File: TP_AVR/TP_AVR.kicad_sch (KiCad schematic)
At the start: 30 parts, among them J1 Conn_02x20_Counter_Clockwise, M1 ProMicro, U1 74HC238, U2 74HC238

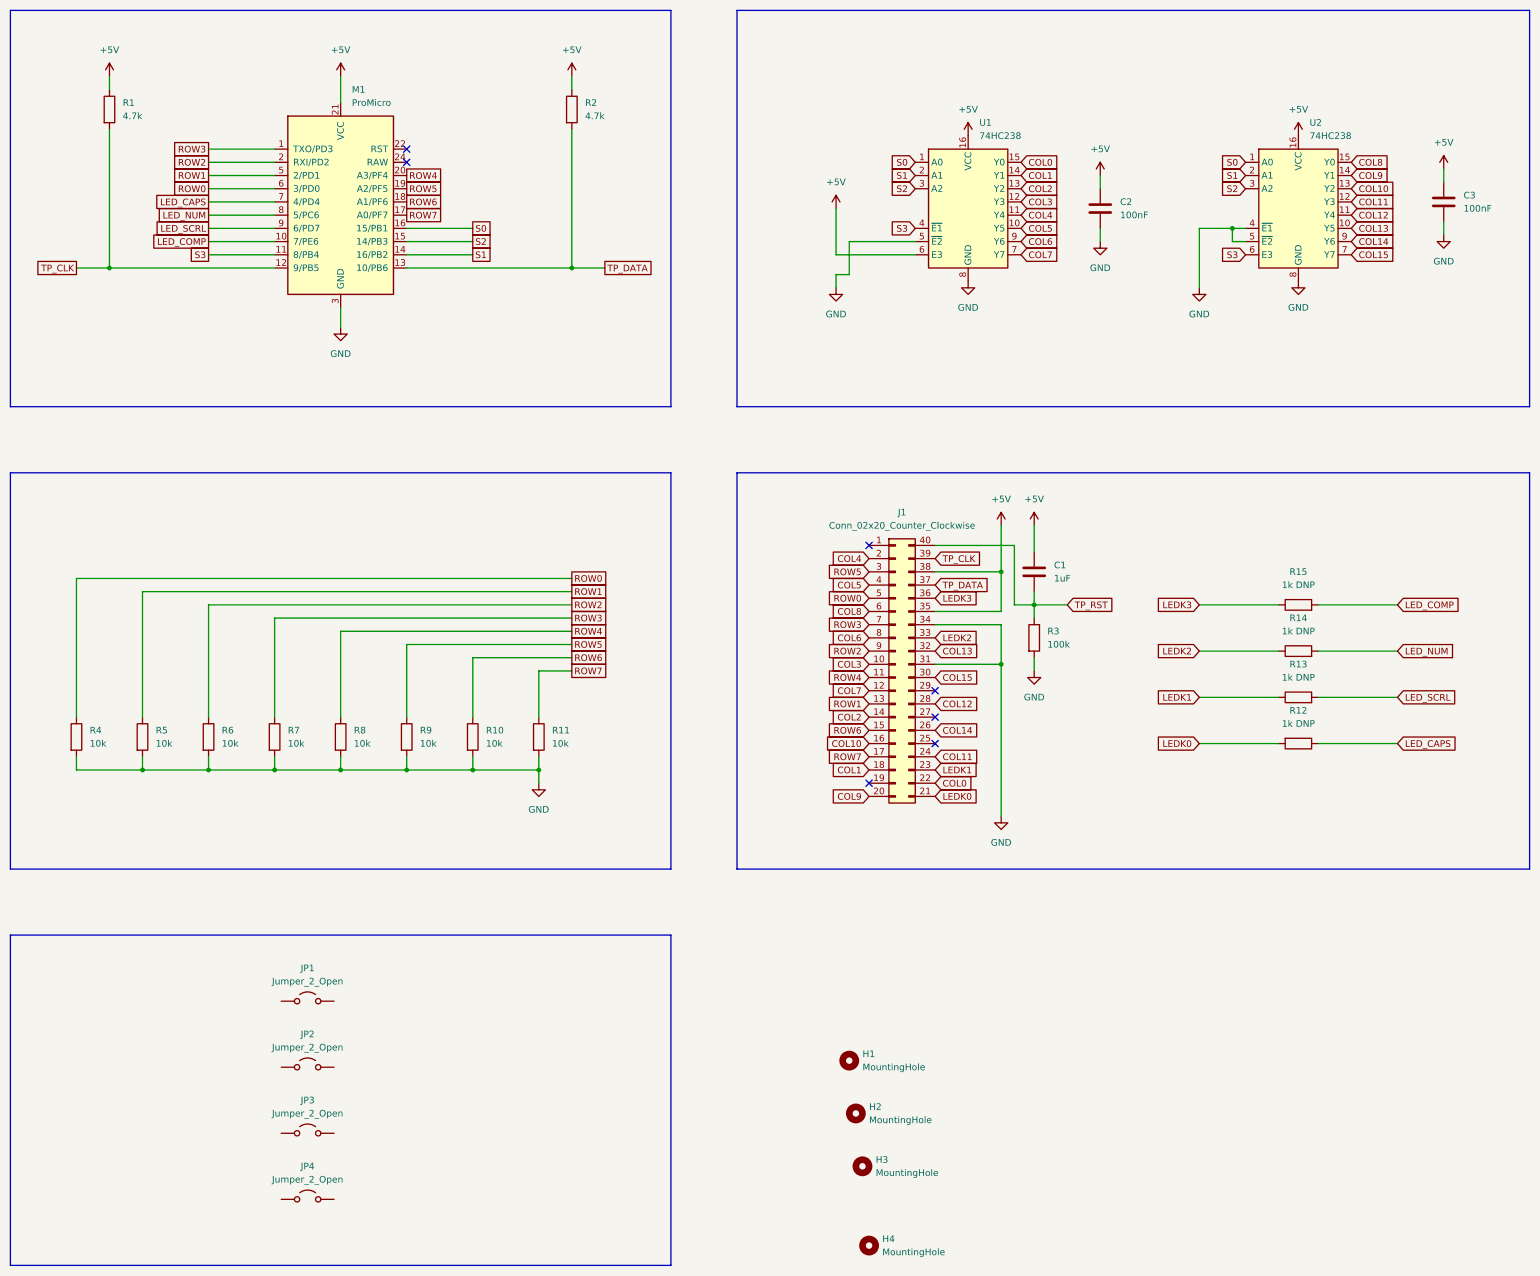
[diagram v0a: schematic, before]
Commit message: Finished up board files
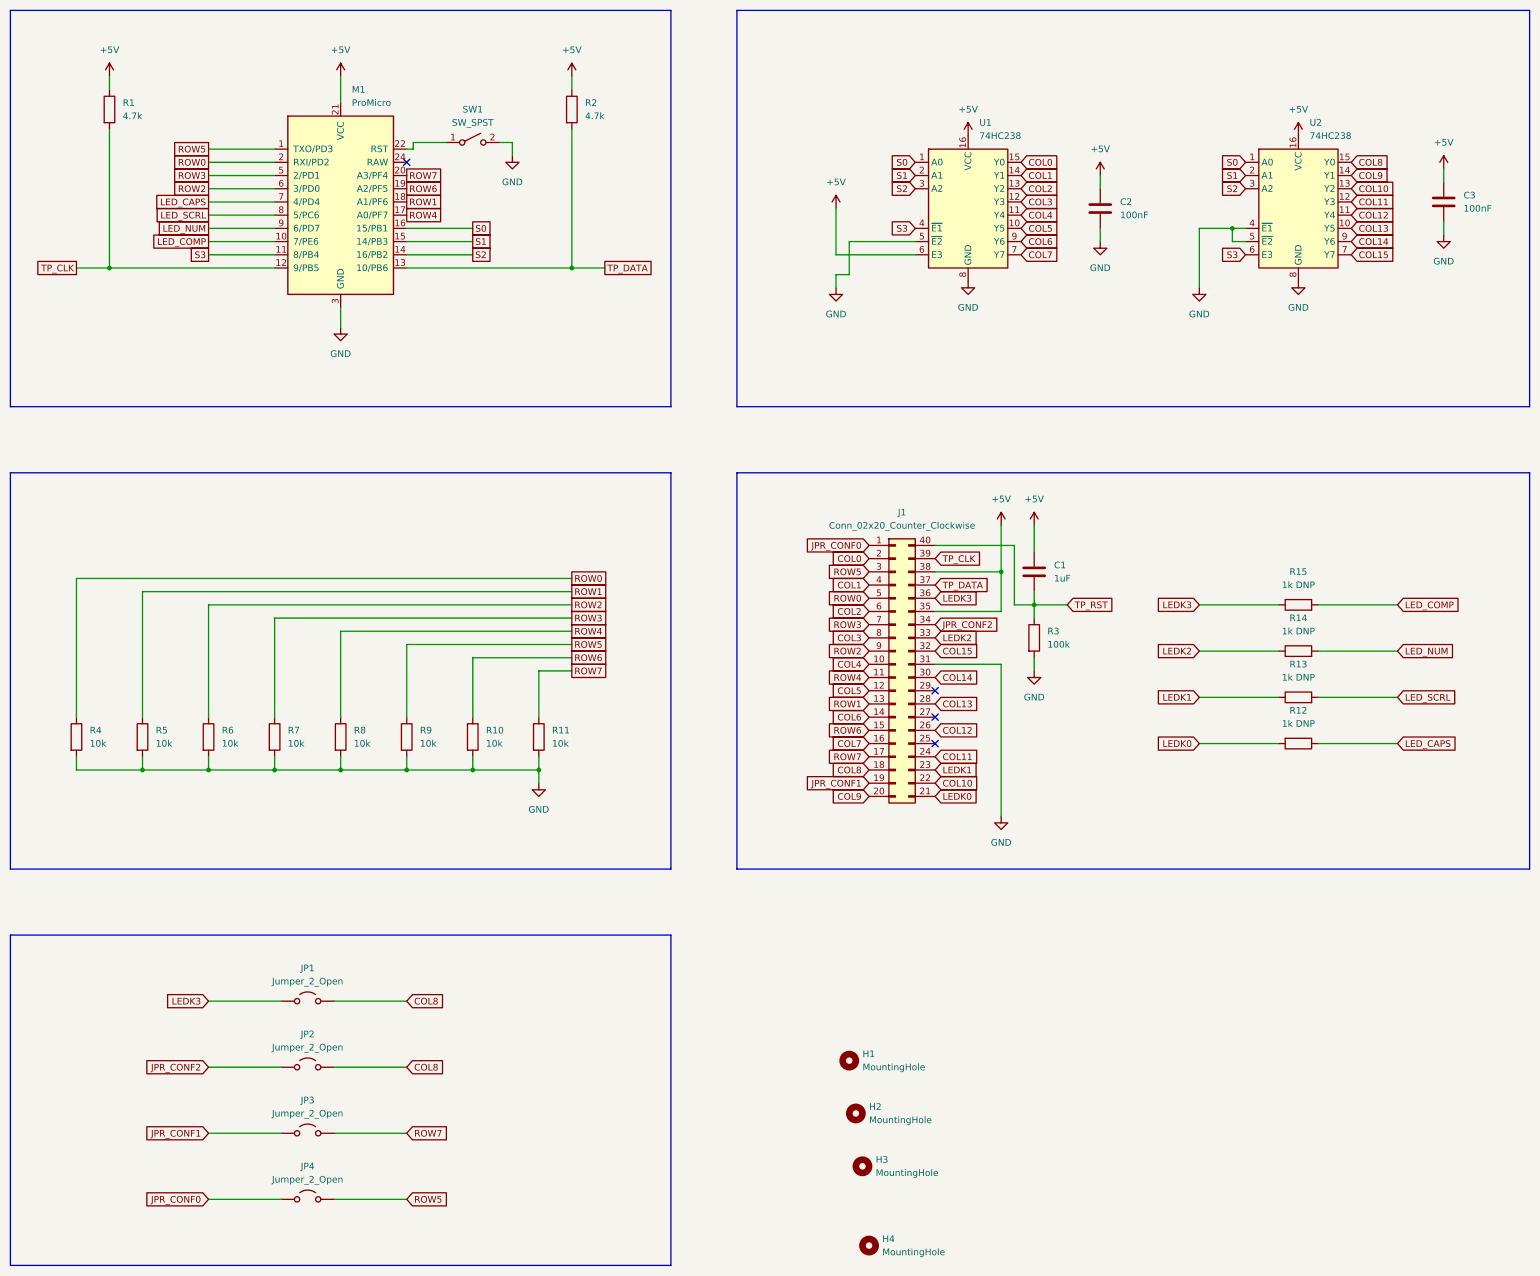
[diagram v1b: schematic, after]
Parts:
- added SW1: SW_SPST, Button_Switch_THT:SW_SPST_Omron_B3F-315x_Angled, symbol Switch:SW_SPST
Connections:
- net COL0: now also J1.2 (Pin_2); no longer J1.22 (Pin_22)
- net COL1: now also J1.4 (Pin_4); no longer J1.18 (Pin_18)
- net COL10: now also J1.22 (Pin_22); no longer J1.16 (Pin_16)
- net COL12: now also J1.26 (Pin_26); no longer J1.28 (Pin_28)
- net COL13: now also J1.28 (Pin_28); no longer J1.32 (Pin_32)
- net COL14: now also J1.30 (Pin_30); no longer J1.26 (Pin_26)
- net COL15: now also J1.32 (Pin_32); no longer J1.30 (Pin_30)
- net COL2: now also J1.6 (Pin_6); no longer J1.14 (Pin_14)
- net COL3: now also J1.8 (Pin_8); no longer J1.10 (Pin_10)
- net COL4: now also J1.10 (Pin_10); no longer J1.2 (Pin_2)
- net COL5: now also J1.12 (Pin_12); no longer J1.4 (Pin_4)
- net COL6: now also J1.14 (Pin_14); no longer J1.8 (Pin_8)
- net COL7: now also J1.16 (Pin_16); no longer J1.12 (Pin_12)
- net COL8: now also J1.18 (Pin_18), JP1.2 (B), JP2.2 (B); no longer J1.6 (Pin_6)
- net GND: now also SW1.2 (B); no longer J1.34 (Pin_34)
- net LEDK3: now also JP1.1 (A)
- net LED_NUM: now also M1.9 (6/PD7); no longer M1.8 (5/PC6)
- net LED_SCRL: now also M1.8 (5/PC6); no longer M1.9 (6/PD7)
- net ROW0: now also M1.2 (RXI/PD2); no longer M1.6 (3/PD0)
- net ROW1: now also M1.18 (A1/PF6); no longer M1.5 (2/PD1)
- net ROW2: now also M1.6 (3/PD0); no longer M1.2 (RXI/PD2)
- net ROW3: now also M1.5 (2/PD1); no longer M1.1 (TXO/PD3)
- net ROW4: now also M1.17 (A0/PF7); no longer M1.20 (A3/PF4)
- net ROW5: now also JP4.2 (B), M1.1 (TXO/PD3); no longer M1.19 (A2/PF5)
- net ROW6: now also M1.19 (A2/PF5); no longer M1.18 (A1/PF6)
- net ROW7: now also JP3.2 (B), M1.20 (A3/PF4); no longer M1.17 (A0/PF7)
- net S1: now also M1.15 (14/PB3); no longer M1.14 (16/PB2)
- net S2: now also M1.14 (16/PB2); no longer M1.15 (14/PB3)
- net JPR_CONF0: now reaches JP4.1 (A)
- net JPR_CONF0: now also J1.1 (Pin_1)
- net at M1.22 (RST): now also SW1.1 (A)
- net JPR_CONF1: now reaches J1.19 (Pin_19)
- net JPR_CONF1: now also JP3.1 (A)
- net JPR_CONF2: now reaches JP2.1 (A)
- net JPR_CONF2: now also J1.34 (Pin_34)
- no-connect marks 7 -> 4

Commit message: bill of materials, board exported
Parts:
- J1: value Conn_02x20_Counter_Clockwise -> JAE_AA01B-S040VA1
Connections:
- net GND: now also SW1.1 (A); no longer SW1.2 (B)
- net at M1.22 (RST): now also SW1.2 (B); no longer SW1.1 (A)
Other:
- company: (none) -> micl.dev
- title: (none) -> TP_AVR_REVERSED
- moved on the sheet: H1, H2, H3, H4
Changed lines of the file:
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@@
 	(generator_version "10.0")
 	(paper "A3")
+	(title_block
+		(title "TP_AVR_REVERSED")
+		(date "2026-06-24")
+		(rev "A")
+		(company "micl.dev")
+	)
 	(rectangle
 		(start 25.4 25.4)
@@
 	(symbol
 		(lib_id "Mechanical:MountingHole")
-		(at 186.69 227.33 0)
+		(at 184.15 209.55 0)
 		(unit 1)
 		(body_style 1)
@@
 		(fields_autoplaced yes)
 		(property "Reference" "H1"
-			(at 189.23 226.0599 0)
+			(at 186.69 208.2799 0)
 			(show_name no)
 			(do_not_autoplace no)
@@
 		)
 		(property "Value" "MountingHole"
-			(at 189.23 228.5999 0)
+			(at 186.69 210.8199 0)
+			(hide yes)
 			(show_name no)
 			(do_not_autoplace no)
@@
 		)
 		(property "Footprint" "MountingHole:MountingHole_2.2mm_M2"
-			(at 186.69 227.33 0)
+			(at 184.15 209.55 0)
 			(hide yes)
 			(show_name no)
@@
 		)
 		(property "Datasheet" ""
-			(at 186.69 227.33 0)
+			(at 184.15 209.55 0)
 			(hide yes)
 			(show_name no)
@@
 		)
 		(property "Description" "Mounting Hole without connection"
-			(at 186.69 227.33 0)
+			(at 184.15 209.55 0)
 			(hide yes)
 			(show_name no)
@@
 	(symbol
 		(lib_id "Mechanical:MountingHole")
-		(at 187.96 237.49 0)
+		(at 196.85 209.55 0)
 		(unit 1)
 		(body_style 1)
@@
 		(fields_autoplaced yes)
 		(property "Reference" "H2"
-			(at 190.5 236.2199 0)
+			(at 199.39 208.2799 0)
 			(show_name no)
 			(do_not_autoplace no)
@@
 		)
 		(property "Value" "MountingHole"
-			(at 190.5 238.7599 0)
+			(at 199.39 210.8199 0)
+			(hide yes)
 			(show_name no)
 			(do_not_autoplace no)
@@
 		)
 		(property "Footprint" "MountingHole:MountingHole_2.2mm_M2"
-			(at 187.96 237.49 0)
+			(at 196.85 209.55 0)
 			(hide yes)
 			(show_name no)
@@
 		)
 		(property "Datasheet" ""
-			(at 187.96 237.49 0)
+			(at 196.85 209.55 0)
 			(hide yes)
 			(show_name no)
@@
 		)
 		(property "Description" "Mounting Hole without connection"
-			(at 187.96 237.49 0)
+			(at 196.85 209.55 0)
 			(hide yes)
 			(show_name no)
@@
 	(symbol
 		(lib_id "Mechanical:MountingHole")
-		(at 189.23 247.65 0)
+		(at 209.55 209.55 0)
 		(unit 1)
 		(body_style 1)
@@
 		(fields_autoplaced yes)
 		(property "Reference" "H3"
-			(at 191.77 246.3799 0)
+			(at 212.09 208.2799 0)
 			(show_name no)
 			(do_not_autoplace no)
@@
 		)
 		(property "Value" "MountingHole"
-			(at 191.77 248.9199 0)
+			(at 212.09 210.8199 0)
+			(hide yes)
 			(show_name no)
 			(do_not_autoplace no)
@@
 		)
 		(property "Footprint" "MountingHole:MountingHole_2.2mm_M2"
-			(at 189.23 247.65 0)
+			(at 209.55 209.55 0)
 			(hide yes)
 			(show_name no)
@@
 		)
 		(property "Datasheet" ""
-			(at 189.23 247.65 0)
+			(at 209.55 209.55 0)
 			(hide yes)
 			(show_name no)
@@
 		)
 		(property "Description" "Mounting Hole without connection"
-			(at 189.23 247.65 0)
+			(at 209.55 209.55 0)
 			(hide yes)
 			(show_name no)
@@
 			)
 		)
-		(property "Value" "Conn_02x20_Counter_Clockwise"
+		(property "Value" "JAE_AA01B-S040VA1"
 			(at 196.85 124.46 0)
 			(show_name no)
@@
 		(lib_id "Switch:SW_SPST")
 		(at 114.3 50.8 0)
+		(mirror y)
 		(unit 1)
 		(body_style 1)
@@
 		(in_pos_files yes)
 		(dnp no)
-		(fields_autoplaced yes)
 		(property "Reference" "SW1"
 			(at 114.3 44.45 0)
@@
 	(symbol
 		(lib_id "Mechanical:MountingHole")
-		(at 190.5 262.89 0)
+		(at 222.25 209.55 0)
 		(unit 1)
 		(body_style 1)
@@
 		(fields_autoplaced yes)
 		(property "Reference" "H4"
-			(at 193.04 261.6199 0)
+			(at 224.79 208.2799 0)
 			(show_name no)
 			(do_not_autoplace no)
@@
 		)
 		(property "Value" "MountingHole"
-			(at 193.04 264.1599 0)
+			(at 224.79 210.8199 0)
+			(hide yes)
 			(show_name no)
 			(do_not_autoplace no)
@@
 		)
 		(property "Footprint" "MountingHole:MountingHole_2.2mm_M2"
-			(at 190.5 262.89 0)
+			(at 222.25 209.55 0)
 			(hide yes)
 			(show_name no)
@@
 		)
 		(property "Datasheet" ""
-			(at 190.5 262.89 0)
+			(at 222.25 209.55 0)
 			(hide yes)
 			(show_name no)
@@
 		)
 		(property "Description" "Mounting Hole without connection"
-			(at 190.5 262.89 0)
+			(at 222.25 209.55 0)
 			(hide yes)
 			(show_name no)
